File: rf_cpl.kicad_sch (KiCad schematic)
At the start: 4 parts, among them J1 Conn_Coaxial

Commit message: Add files via upload
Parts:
- renumbered J1 to J2, U6 to U7, U7 to U8, U8 to U9
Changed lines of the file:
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@@
   (symbol (lib_id "power:GND") (at 182.88 154.94 0) (unit 1)
     (in_bom yes) (on_board yes) (dnp no) (fields_autoplaced)
-    (property "Reference" "#PWR018" (at 182.88 161.29 0)
+    (property "Reference" "#PWR048" (at 182.88 161.29 0)
       (effects (font (size 1.27 1.27)) hide)
     )
@@
       (project "m17-rru-rf"
         (path "/4c42207c-9e6b-42da-ad38-da126b892014/59b2721c-5b8a-4fc3-bf5e-590dec787afb"
-          (reference "#PWR018") (unit 1)
+          (reference "#PWR048") (unit 1)
         )
       )
@@
   (symbol (lib_id "power:GND") (at 242.57 135.89 0) (unit 1)
     (in_bom yes) (on_board yes) (dnp no) (fields_autoplaced)
-    (property "Reference" "#PWR021" (at 242.57 142.24 0)
+    (property "Reference" "#PWR051" (at 242.57 142.24 0)
       (effects (font (size 1.27 1.27)) hide)
     )
@@
       (project "m17-rru-rf"
         (path "/4c42207c-9e6b-42da-ad38-da126b892014/59b2721c-5b8a-4fc3-bf5e-590dec787afb"
-          (reference "#PWR021") (unit 1)
+          (reference "#PWR051") (unit 1)
         )
       )
@@
   (symbol (lib_id "Parts:GAT-30+") (at 223.52 151.13 270) (unit 1)
     (in_bom yes) (on_board yes) (dnp no) (fields_autoplaced)
-    (property "Reference" "U8" (at 229.235 151.13 90)
+    (property "Reference" "U9" (at 229.235 151.13 90)
       (effects (font (size 1.27 1.27)) (justify left))
     )
@@
       (project "m17-rru-rf"
         (path "/4c42207c-9e6b-42da-ad38-da126b892014/59b2721c-5b8a-4fc3-bf5e-590dec787afb"
-          (reference "U8") (unit 1)
+          (reference "U9") (unit 1)
         )
       )
@@
   (symbol (lib_id "Connector:Conn_Coaxial") (at 242.57 129.54 0) (unit 1)
     (in_bom yes) (on_board yes) (dnp no) (fields_autoplaced)
-    (property "Reference" "J1" (at 245.1101 128.6211 0)
+    (property "Reference" "J2" (at 245.1101 128.6211 0)
       (effects (font (size 1.27 1.27)) (justify left))
     )
@@
       (project "m17-rru-rf"
         (path "/4c42207c-9e6b-42da-ad38-da126b892014/59b2721c-5b8a-4fc3-bf5e-590dec787afb"
-          (reference "J1") (unit 1)
+          (reference "J2") (unit 1)
         )
       )
@@
   (symbol (lib_id "Parts:GAT-30+") (at 193.04 151.13 270) (unit 1)
     (in_bom yes) (on_board yes) (dnp no) (fields_autoplaced)
-    (property "Reference" "U6" (at 198.755 151.13 90)
+    (property "Reference" "U7" (at 198.755 151.13 90)
       (effects (font (size 1.27 1.27)) (justify left))
     )
@@
       (project "m17-rru-rf"
         (path "/4c42207c-9e6b-42da-ad38-da126b892014/59b2721c-5b8a-4fc3-bf5e-590dec787afb"
-          (reference "U6") (unit 1)
+          (reference "U7") (unit 1)
         )
       )
@@
   (symbol (lib_id "Parts:SYBD-30-62HP+") (at 208.28 127 0) (mirror y) (unit 1)
     (in_bom yes) (on_board yes) (dnp no)
-    (property "Reference" "U7" (at 208.28 125.4069 0)
+    (property "Reference" "U8" (at 208.28 125.4069 0)
       (effects (font (size 1.27 1.27)))
     )
@@
       (project "m17-rru-rf"
         (path "/4c42207c-9e6b-42da-ad38-da126b892014/59b2721c-5b8a-4fc3-bf5e-590dec787afb"
-          (reference "U7") (unit 1)
+          (reference "U8") (unit 1)
         )
       )
@@
   (symbol (lib_id "power:GND") (at 208.28 138.43 0) (unit 1)
     (in_bom yes) (on_board yes) (dnp no) (fields_autoplaced)
-    (property "Reference" "#PWR019" (at 208.28 144.78 0)
+    (property "Reference" "#PWR049" (at 208.28 144.78 0)
       (effects (font (size 1.27 1.27)) hide)
     )
@@
       (project "m17-rru-rf"
         (path "/4c42207c-9e6b-42da-ad38-da126b892014/59b2721c-5b8a-4fc3-bf5e-590dec787afb"
-          (reference "#PWR019") (unit 1)
+          (reference "#PWR049") (unit 1)
         )
       )
@@
   (symbol (lib_id "power:GND") (at 213.36 154.94 0) (unit 1)
     (in_bom yes) (on_board yes) (dnp no) (fields_autoplaced)
-    (property "Reference" "#PWR020" (at 213.36 161.29 0)
+    (property "Reference" "#PWR050" (at 213.36 161.29 0)
       (effects (font (size 1.27 1.27)) hide)
     )
@@
       (project "m17-rru-rf"
         (path "/4c42207c-9e6b-42da-ad38-da126b892014/59b2721c-5b8a-4fc3-bf5e-590dec787afb"
-          (reference "#PWR020") (unit 1)
+          (reference "#PWR050") (unit 1)
         )
       )

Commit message: Add files via upload
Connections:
- net FWD_SENSE renamed FWD_RF
- net REF_SENSE renamed REF_RF
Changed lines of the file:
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@@
     (effects (font (size 1.27 1.27)) (justify left bottom))
   )
-  (hierarchical_label "REF_SENSE" (shape output) (at 193.04 165.1 270) (fields_autoplaced)
+  (hierarchical_label "REF_RF" (shape output) (at 193.04 165.1 270) (fields_autoplaced)
     (effects (font (size 1.27 1.27)) (justify right))
   )
@@
     (effects (font (size 1.27 1.27)) (justify right))
   )
-  (hierarchical_label "FWD_SENSE" (shape output) (at 223.52 165.1 270) (fields_autoplaced)
+  (hierarchical_label "FWD_RF" (shape output) (at 223.52 165.1 270) (fields_autoplaced)
     (effects (font (size 1.27 1.27)) (justify right))
   )

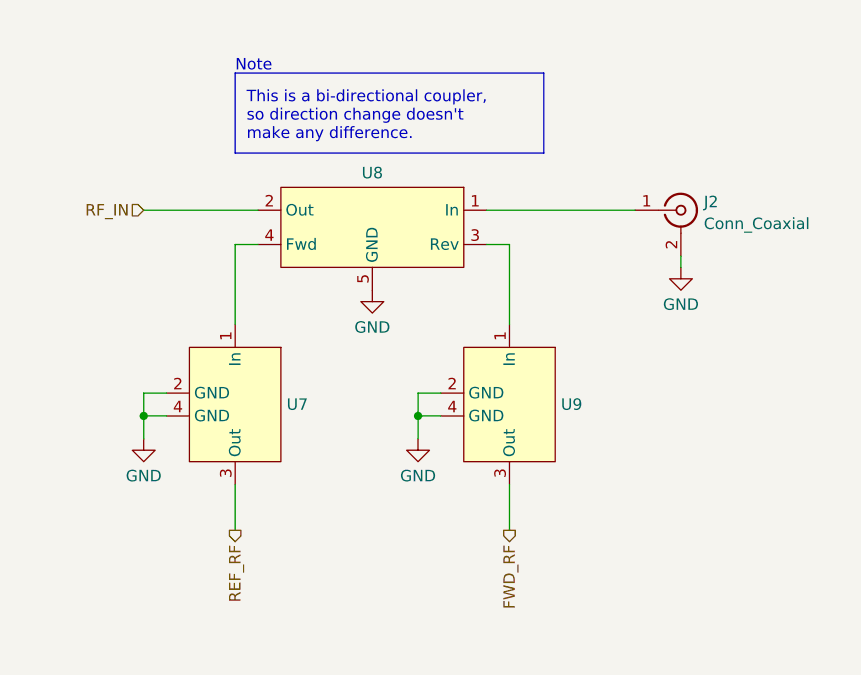
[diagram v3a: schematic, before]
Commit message: significant updates
- supply for the detector block changed from 3.3V to 5V
- minor bugfixes
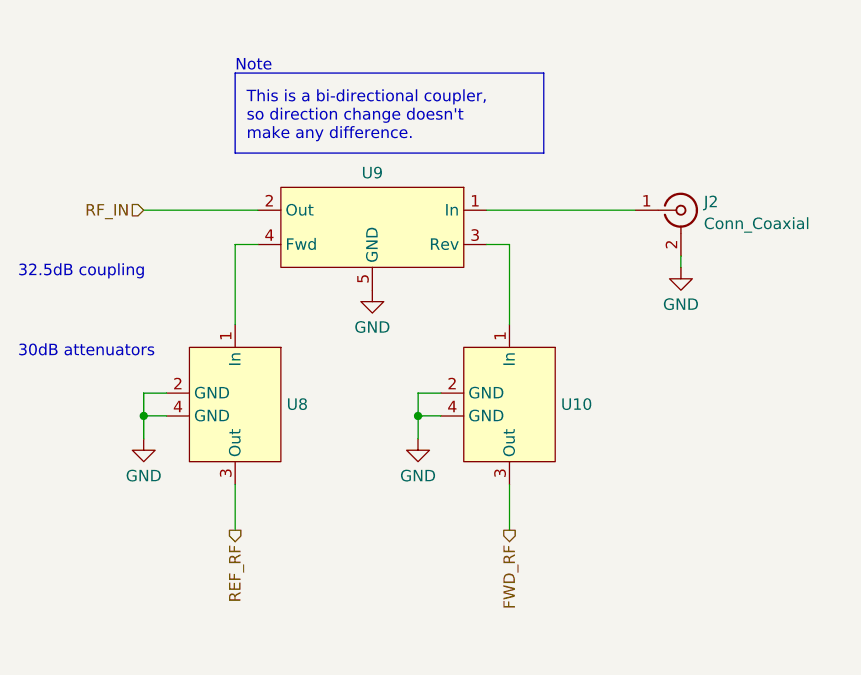
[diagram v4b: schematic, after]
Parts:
- renumbered U9 to U10, U7 to U8, U8 to U9
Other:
- note added: "30dB attenuators"
- note added: "32.5dB coupling"
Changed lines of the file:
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@@
+    (effects (font (size 1.27 1.27)) (justify left bottom))
+  )
+  (text "30dB attenuators" (at 168.91 146.05 0)
     (effects (font (size 1.27 1.27)) (justify left bottom))
   )
@@
     (effects (font (size 1.27 1.27)) (justify left bottom))
   )
+  (text "32.5dB coupling" (at 168.91 137.16 0)
+    (effects (font (size 1.27 1.27)) (justify left bottom))
+  )
   (hierarchical_label "REF_RF" (shape output) (at 193.04 165.1 270) (fields_autoplaced)
     (effects (font (size 1.27 1.27)) (justify right))
@@
   (symbol (lib_id "power:GND") (at 182.88 154.94 0) (unit 1)
     (in_bom yes) (on_board yes) (dnp no) (fields_autoplaced)
-    (property "Reference" "#PWR047" (at 182.88 161.29 0)
+    (property "Reference" "#PWR052" (at 182.88 161.29 0)
       (effects (font (size 1.27 1.27)) hide)
     )
@@
       (project "m17-rru-rf"
         (path "/4c42207c-9e6b-42da-ad38-da126b892014/59b2721c-5b8a-4fc3-bf5e-590dec787afb"
-          (reference "#PWR047") (unit 1)
+          (reference "#PWR052") (unit 1)
         )
       )
@@
   (symbol (lib_id "power:GND") (at 242.57 135.89 0) (unit 1)
     (in_bom yes) (on_board yes) (dnp no) (fields_autoplaced)
-    (property "Reference" "#PWR050" (at 242.57 142.24 0)
+    (property "Reference" "#PWR055" (at 242.57 142.24 0)
       (effects (font (size 1.27 1.27)) hide)
     )
@@
       (project "m17-rru-rf"
         (path "/4c42207c-9e6b-42da-ad38-da126b892014/59b2721c-5b8a-4fc3-bf5e-590dec787afb"
-          (reference "#PWR050") (unit 1)
+          (reference "#PWR055") (unit 1)
         )
       )
@@
   (symbol (lib_id "Parts:GAT-30+") (at 223.52 151.13 270) (unit 1)
     (in_bom yes) (on_board yes) (dnp no) (fields_autoplaced)
-    (property "Reference" "U9" (at 229.235 151.13 90)
+    (property "Reference" "U10" (at 229.235 151.13 90)
       (effects (font (size 1.27 1.27)) (justify left))
     )
@@
       (project "m17-rru-rf"
         (path "/4c42207c-9e6b-42da-ad38-da126b892014/59b2721c-5b8a-4fc3-bf5e-590dec787afb"
-          (reference "U9") (unit 1)
+          (reference "U10") (unit 1)
         )
       )
@@
   (symbol (lib_id "Parts:GAT-30+") (at 193.04 151.13 270) (unit 1)
     (in_bom yes) (on_board yes) (dnp no) (fields_autoplaced)
-    (property "Reference" "U7" (at 198.755 151.13 90)
+    (property "Reference" "U8" (at 198.755 151.13 90)
       (effects (font (size 1.27 1.27)) (justify left))
     )
@@
       (project "m17-rru-rf"
         (path "/4c42207c-9e6b-42da-ad38-da126b892014/59b2721c-5b8a-4fc3-bf5e-590dec787afb"
-          (reference "U7") (unit 1)
+          (reference "U8") (unit 1)
         )
       )
@@
   (symbol (lib_id "Parts:SYBD-30-62HP+") (at 208.28 127 0) (mirror y) (unit 1)
     (in_bom yes) (on_board yes) (dnp no)
-    (property "Reference" "U8" (at 208.28 125.4069 0)
+    (property "Reference" "U9" (at 208.28 125.4069 0)
       (effects (font (size 1.27 1.27)))
     )
@@
       (project "m17-rru-rf"
         (path "/4c42207c-9e6b-42da-ad38-da126b892014/59b2721c-5b8a-4fc3-bf5e-590dec787afb"
-          (reference "U8") (unit 1)
+          (reference "U9") (unit 1)
         )
       )
@@
   (symbol (lib_id "power:GND") (at 208.28 138.43 0) (unit 1)
     (in_bom yes) (on_board yes) (dnp no) (fields_autoplaced)
-    (property "Reference" "#PWR048" (at 208.28 144.78 0)
+    (property "Reference" "#PWR053" (at 208.28 144.78 0)
       (effects (font (size 1.27 1.27)) hide)
     )
@@
       (project "m17-rru-rf"
         (path "/4c42207c-9e6b-42da-ad38-da126b892014/59b2721c-5b8a-4fc3-bf5e-590dec787afb"
-          (reference "#PWR048") (unit 1)
+          (reference "#PWR053") (unit 1)
         )
       )
@@
   (symbol (lib_id "power:GND") (at 213.36 154.94 0) (unit 1)
     (in_bom yes) (on_board yes) (dnp no) (fields_autoplaced)
-    (property "Reference" "#PWR049" (at 213.36 161.29 0)
+    (property "Reference" "#PWR054" (at 213.36 161.29 0)
       (effects (font (size 1.27 1.27)) hide)
     )
@@
       (project "m17-rru-rf"
         (path "/4c42207c-9e6b-42da-ad38-da126b892014/59b2721c-5b8a-4fc3-bf5e-590dec787afb"
-          (reference "#PWR049") (unit 1)
-        )
-      )
+          (reference "#PWR054") (unit 1)
+        )
+      )

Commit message: PN update
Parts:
- J2: PN (none) -> -
- U10, U8: value ~ -> GAT-30+; PN (none) -> -
- U9: value ~ -> SYBD-30-62HP+; PN (none) -> -
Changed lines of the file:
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@@
       (effects (font (size 1.27 1.27)) (justify left))
     )
-    (property "Value" "~" (at 223.52 151.13 0)
+    (property "Value" "GAT-30+" (at 223.52 151.13 0)
       (effects (font (size 1.27 1.27)))
     )
@@
     )
     (property "Datasheet" "" (at 223.52 151.13 0)
+      (effects (font (size 1.27 1.27)) hide)
+    )
+    (property "PN" "-" (at 223.52 151.13 0)
       (effects (font (size 1.27 1.27)) hide)
     )
@@
       (effects (font (size 1.27 1.27)) hide)
     )
+    (property "PN" "-" (at 242.57 129.54 0)
+      (effects (font (size 1.27 1.27)) hide)
+    )
     (pin "1")
     (pin "2")
@@
       (effects (font (size 1.27 1.27)) (justify left))
     )
-    (property "Value" "~" (at 193.04 151.13 0)
+    (property "Value" "GAT-30+" (at 193.04 151.13 0)
       (effects (font (size 1.27 1.27)))
     )
@@
     )
     (property "Datasheet" "" (at 193.04 151.13 0)
+      (effects (font (size 1.27 1.27)) hide)
+    )
+    (property "PN" "-" (at 193.04 151.13 0)
       (effects (font (size 1.27 1.27)) hide)
     )
@@
       (effects (font (size 1.27 1.27)))
     )
-    (property "Value" "~" (at 208.28 127 0)
+    (property "Value" "SYBD-30-62HP+" (at 208.28 127 0)
       (effects (font (size 1.27 1.27)))
     )
@@
       (effects (font (size 1.27 1.27)) hide)
     )
+    (property "PN" "-" (at 208.28 127 0)
+      (effects (font (size 1.27 1.27)) hide)
+    )

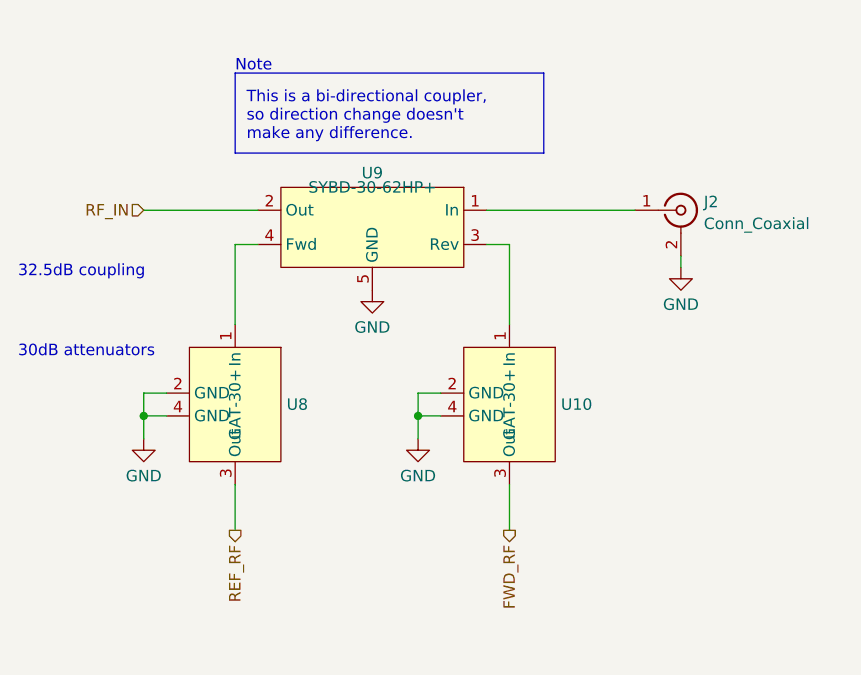
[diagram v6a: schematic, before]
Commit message: `PWR_FLAG`, ERC cleanup
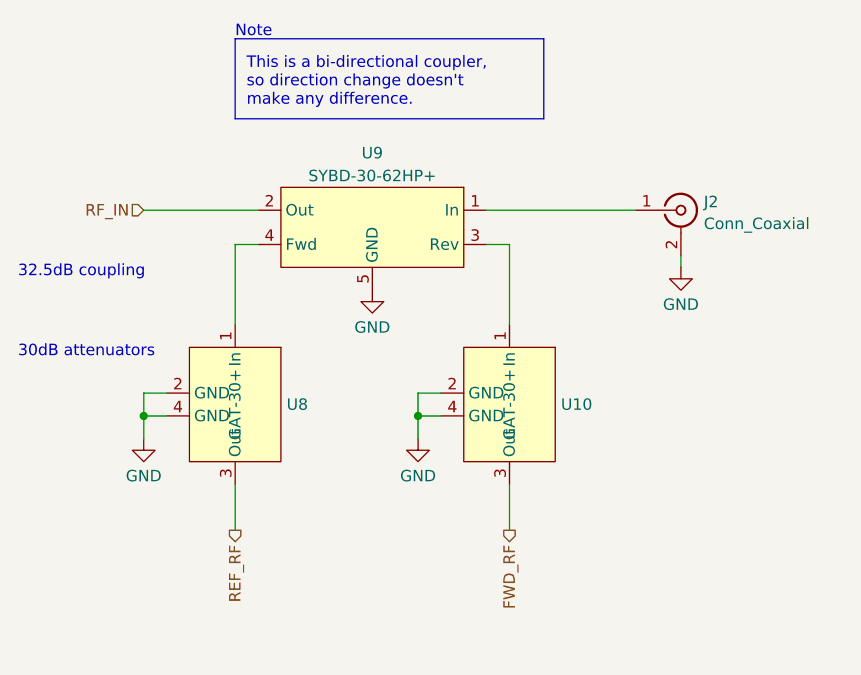
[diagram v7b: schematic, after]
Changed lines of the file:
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@@
     (stroke (width 0) (type default))
   )
-  (rectangle (start 193.04 114.3) (end 227.33 123.19)
+  (rectangle (start 193.04 110.49) (end 227.33 119.38)
     (stroke (width 0) (type default))
     (fill (type none))
   )
-  (text "Note" (at 193.04 114.3 0)
+  (text "Note" (at 193.04 110.49 0)
     (effects (font (size 1.27 1.27)) (justify left bottom))
   )
@@
   )
   (text "This is a bi-directional coupler,\nso direction change doesn't\nmake any difference."
-    (at 194.31 121.92 0)
+    (at 194.31 118.11 0)
     (effects (font (size 1.27 1.27)) (justify left bottom))
   )
@@
   (symbol (lib_id "Parts:SYBD-30-62HP+") (at 208.28 127 0) (mirror y) (unit 1)
     (in_bom yes) (on_board yes) (dnp no)
-    (property "Reference" "U9" (at 208.28 125.4069 0)
+    (property "Reference" "U9" (at 208.28 123.19 0)
       (effects (font (size 1.27 1.27)))
     )
-    (property "Value" "SYBD-30-62HP+" (at 208.28 127 0)
+    (property "Value" "SYBD-30-62HP+" (at 208.28 125.73 0)
       (effects (font (size 1.27 1.27)))
     )

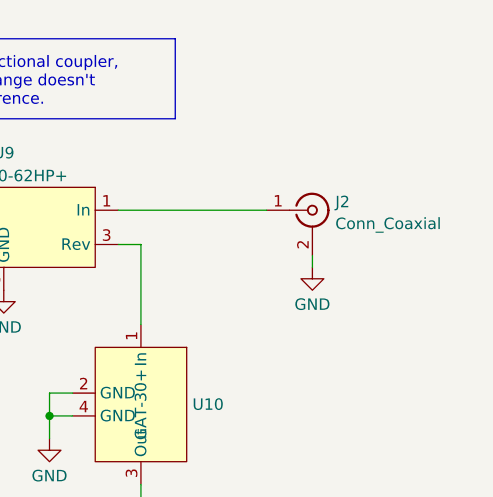
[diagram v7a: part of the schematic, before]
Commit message: TP updates, temp sensor added
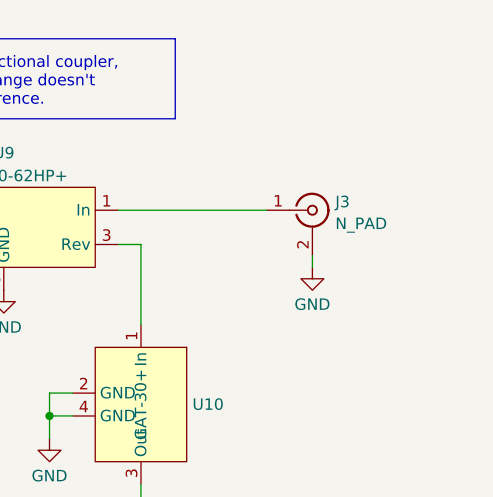
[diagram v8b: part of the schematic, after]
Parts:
- J3: renamed from J2; value Conn_Coaxial -> N_PAD
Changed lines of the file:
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@@
   (symbol (lib_id "power:GND") (at 182.88 154.94 0) (unit 1)
     (in_bom yes) (on_board yes) (dnp no) (fields_autoplaced)
-    (property "Reference" "#PWR052" (at 182.88 161.29 0)
+    (property "Reference" "#PWR056" (at 182.88 161.29 0)
       (effects (font (size 1.27 1.27)) hide)
     )
@@
       (project "m17-rru-rf"
         (path "/4c42207c-9e6b-42da-ad38-da126b892014/59b2721c-5b8a-4fc3-bf5e-590dec787afb"
-          (reference "#PWR052") (unit 1)
+          (reference "#PWR056") (unit 1)
         )
       )
@@
   (symbol (lib_id "power:GND") (at 242.57 135.89 0) (unit 1)
     (in_bom yes) (on_board yes) (dnp no) (fields_autoplaced)
-    (property "Reference" "#PWR055" (at 242.57 142.24 0)
+    (property "Reference" "#PWR059" (at 242.57 142.24 0)
       (effects (font (size 1.27 1.27)) hide)
     )
@@
       (project "m17-rru-rf"
         (path "/4c42207c-9e6b-42da-ad38-da126b892014/59b2721c-5b8a-4fc3-bf5e-590dec787afb"
-          (reference "#PWR055") (unit 1)
+          (reference "#PWR059") (unit 1)
         )
       )
@@
   (symbol (lib_id "Connector:Conn_Coaxial") (at 242.57 129.54 0) (unit 1)
     (in_bom yes) (on_board yes) (dnp no) (fields_autoplaced)
-    (property "Reference" "J2" (at 245.1101 128.6211 0)
-      (effects (font (size 1.27 1.27)) (justify left))
-    )
-    (property "Value" "Conn_Coaxial" (at 245.1101 131.0453 0)
+    (property "Reference" "J3" (at 245.1101 128.6211 0)
+      (effects (font (size 1.27 1.27)) (justify left))
+    )
+    (property "Value" "N_PAD" (at 245.1101 131.0453 0)
       (effects (font (size 1.27 1.27)) (justify left))
     )
@@
       (project "m17-rru-rf"
         (path "/4c42207c-9e6b-42da-ad38-da126b892014/59b2721c-5b8a-4fc3-bf5e-590dec787afb"
-          (reference "J2") (unit 1)
+          (reference "J3") (unit 1)
         )
       )
@@
   (symbol (lib_id "power:GND") (at 208.28 138.43 0) (unit 1)
     (in_bom yes) (on_board yes) (dnp no) (fields_autoplaced)
-    (property "Reference" "#PWR053" (at 208.28 144.78 0)
+    (property "Reference" "#PWR057" (at 208.28 144.78 0)
       (effects (font (size 1.27 1.27)) hide)
     )
@@
       (project "m17-rru-rf"
         (path "/4c42207c-9e6b-42da-ad38-da126b892014/59b2721c-5b8a-4fc3-bf5e-590dec787afb"
-          (reference "#PWR053") (unit 1)
+          (reference "#PWR057") (unit 1)
         )
       )
@@
   (symbol (lib_id "power:GND") (at 213.36 154.94 0) (unit 1)
     (in_bom yes) (on_board yes) (dnp no) (fields_autoplaced)
-    (property "Reference" "#PWR054" (at 213.36 161.29 0)
+    (property "Reference" "#PWR058" (at 213.36 161.29 0)
       (effects (font (size 1.27 1.27)) hide)
     )
@@
       (project "m17-rru-rf"
         (path "/4c42207c-9e6b-42da-ad38-da126b892014/59b2721c-5b8a-4fc3-bf5e-590dec787afb"
-          (reference "#PWR054") (unit 1)
-        )
-      )
+          (reference "#PWR058") (unit 1)
+        )
+      )
